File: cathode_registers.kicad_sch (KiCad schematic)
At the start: 10 parts, among them U3 74HC595, U4 74HC595, U5 74HC595, U6 74HC595, U7 74HC595

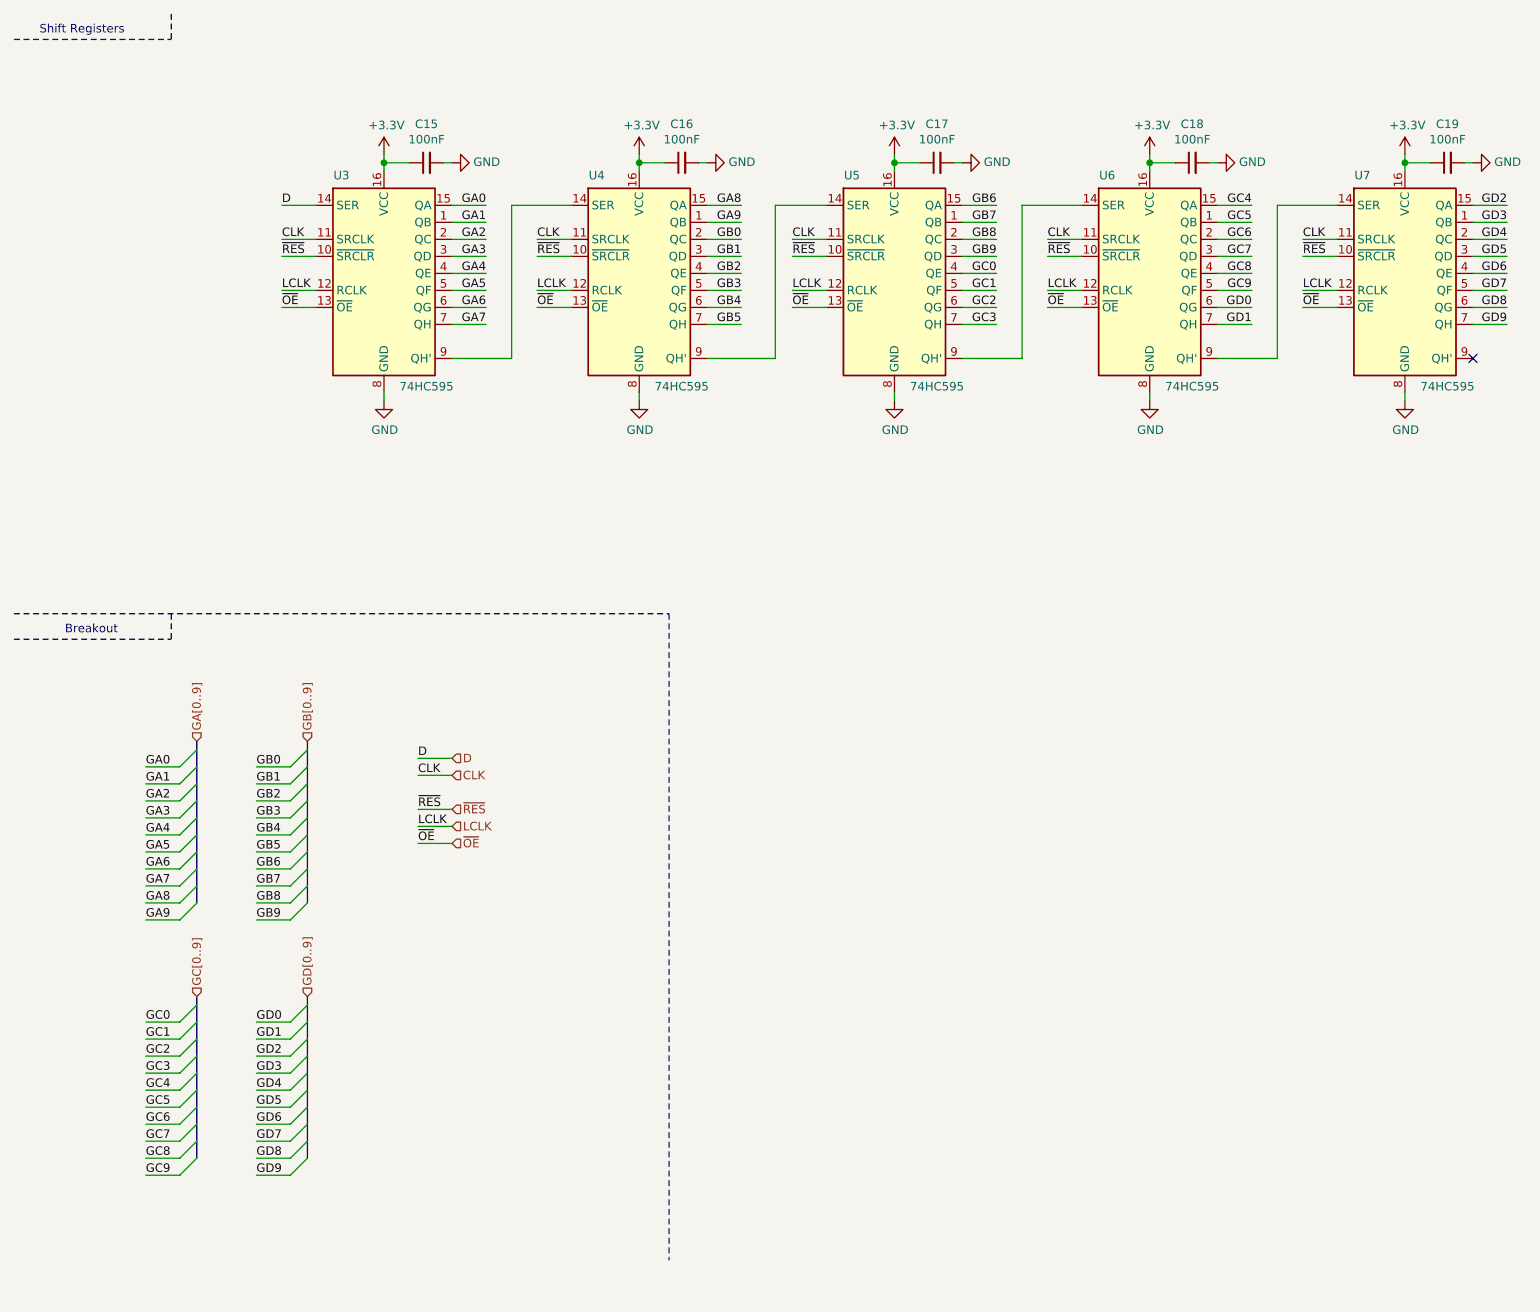
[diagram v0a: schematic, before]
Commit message: added outputs for schematic and gerber view
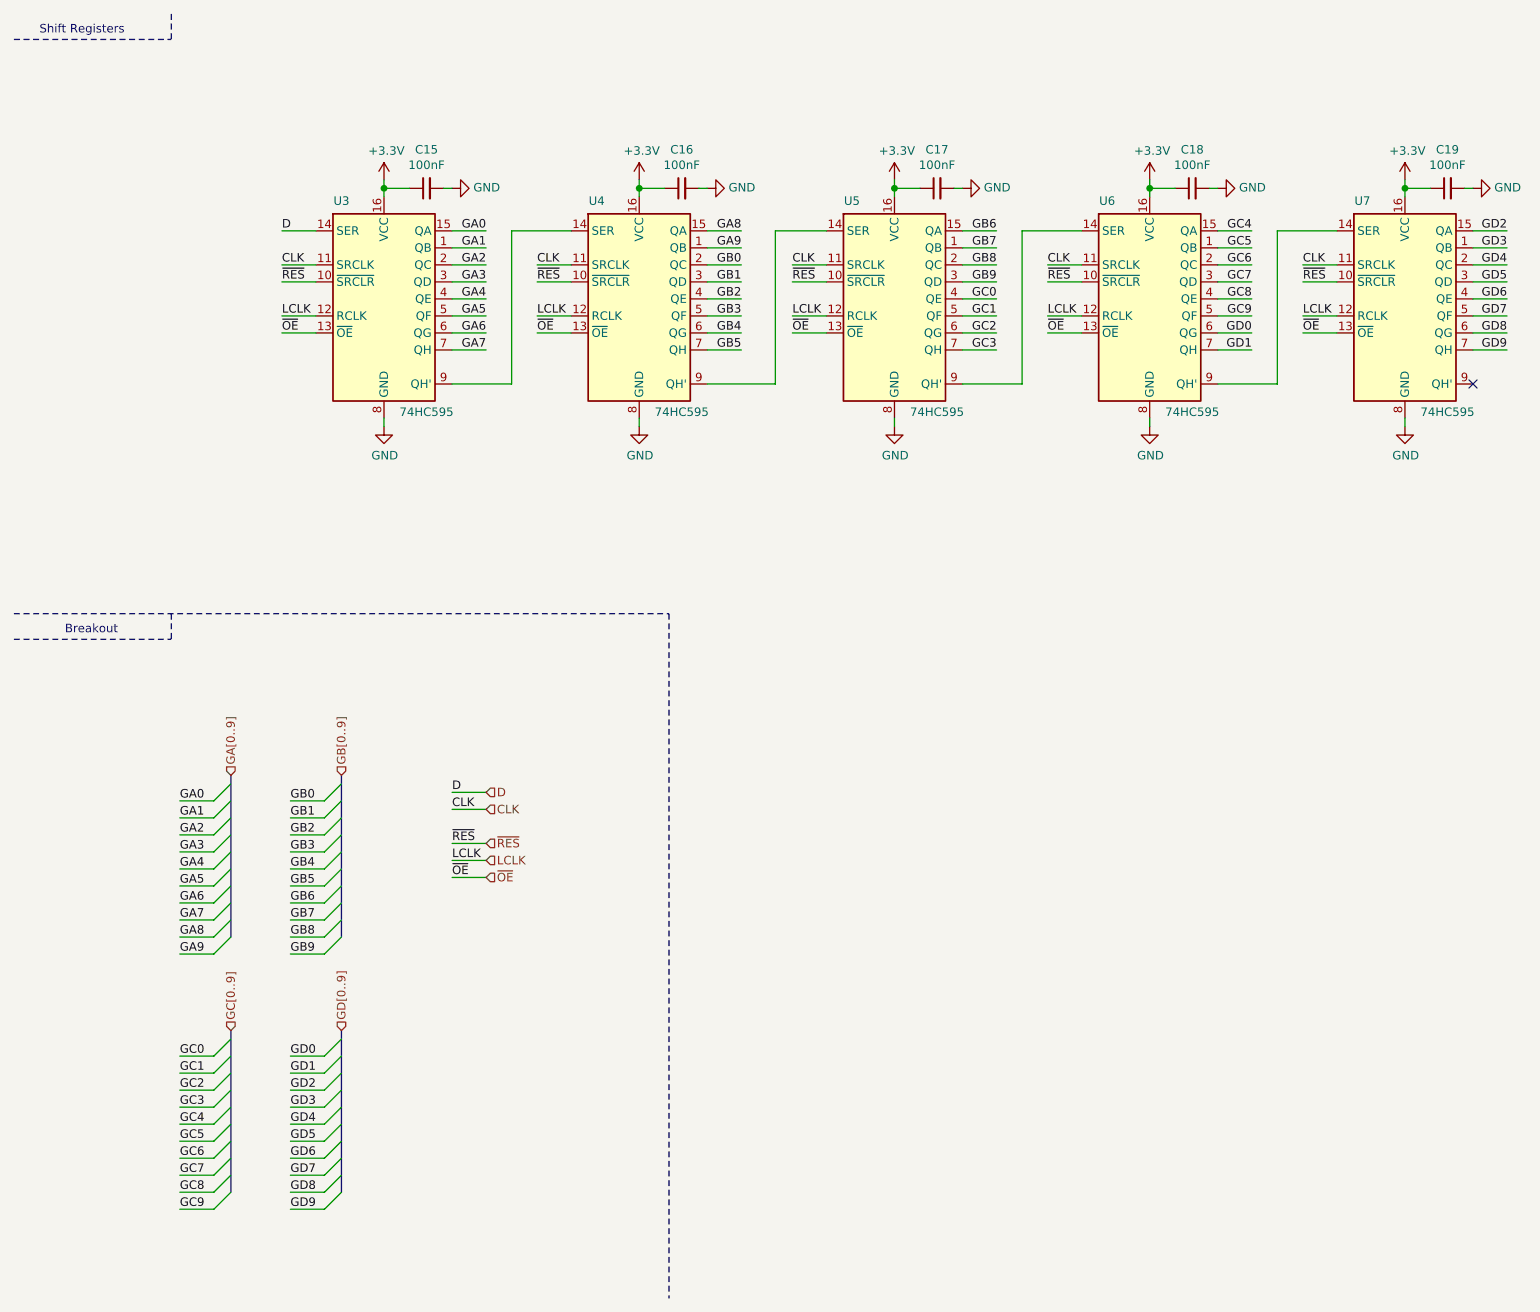
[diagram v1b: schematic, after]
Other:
- moved on the sheet: C15, C16, C17, C18, C19, U3, U4, U5, U6, U7
